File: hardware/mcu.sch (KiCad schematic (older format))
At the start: 27 parts

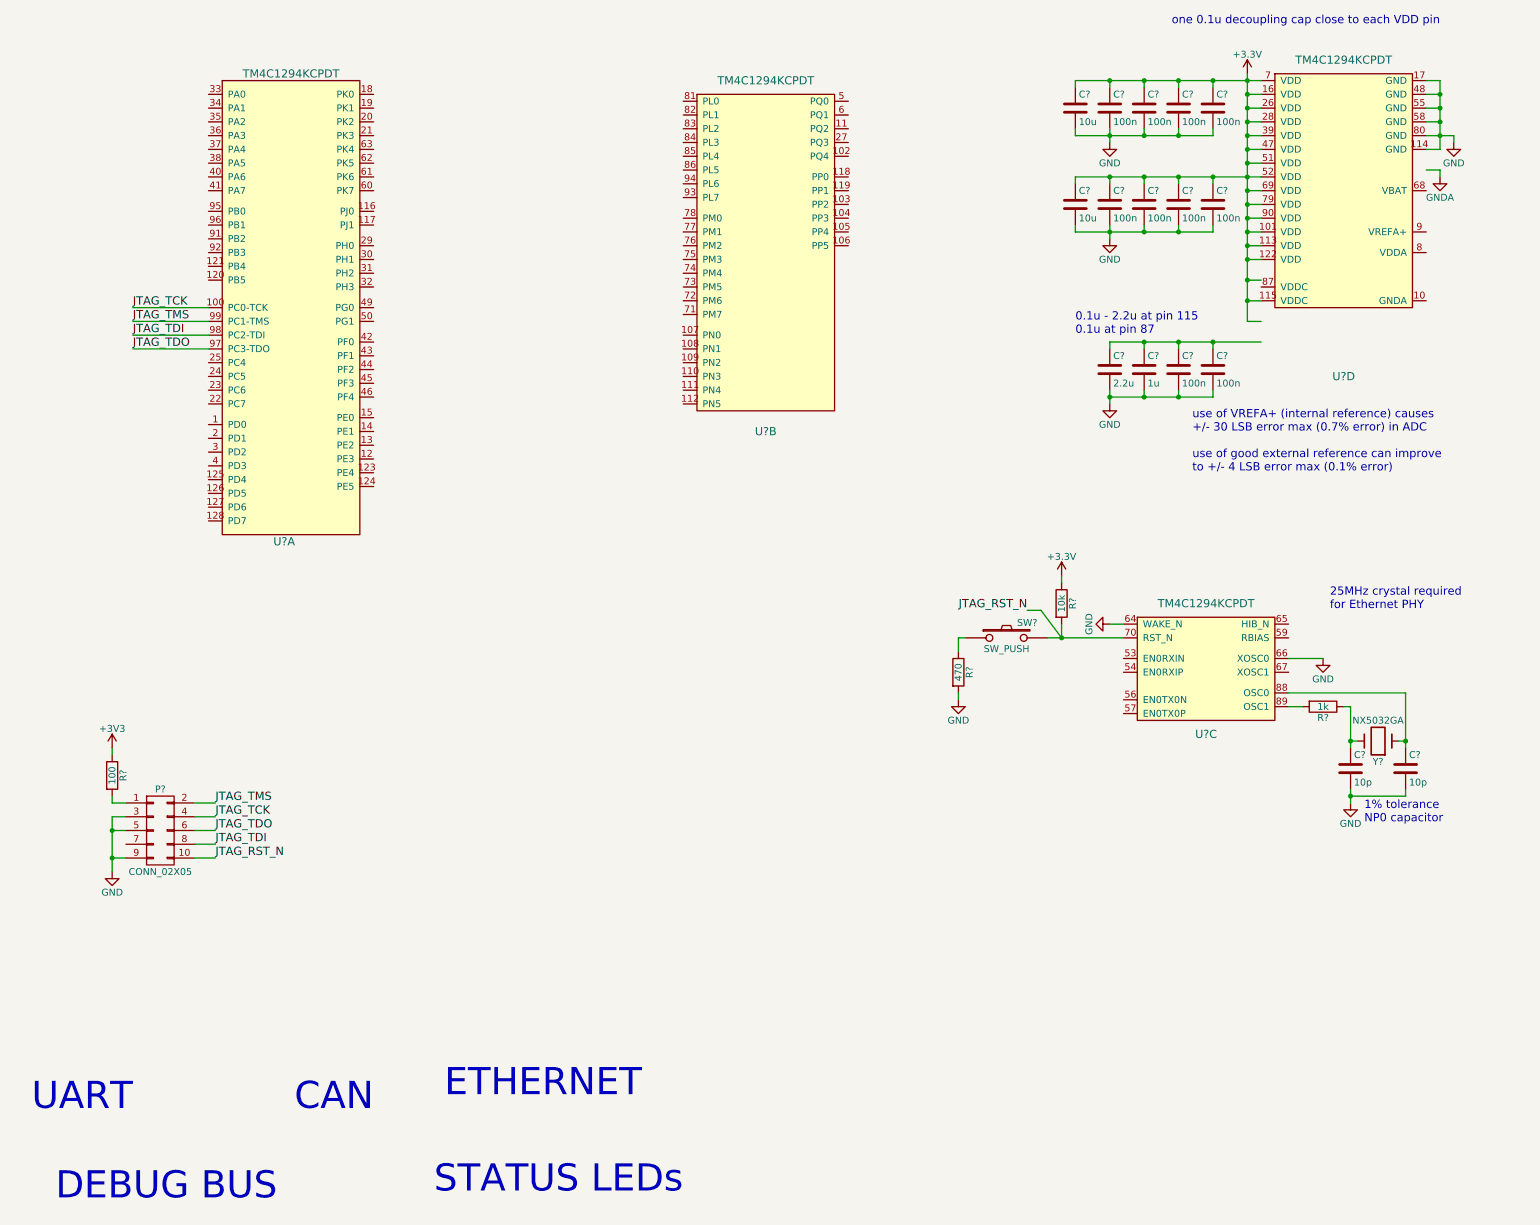
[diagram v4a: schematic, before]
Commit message: ERC cleanup, begin pcbnew population
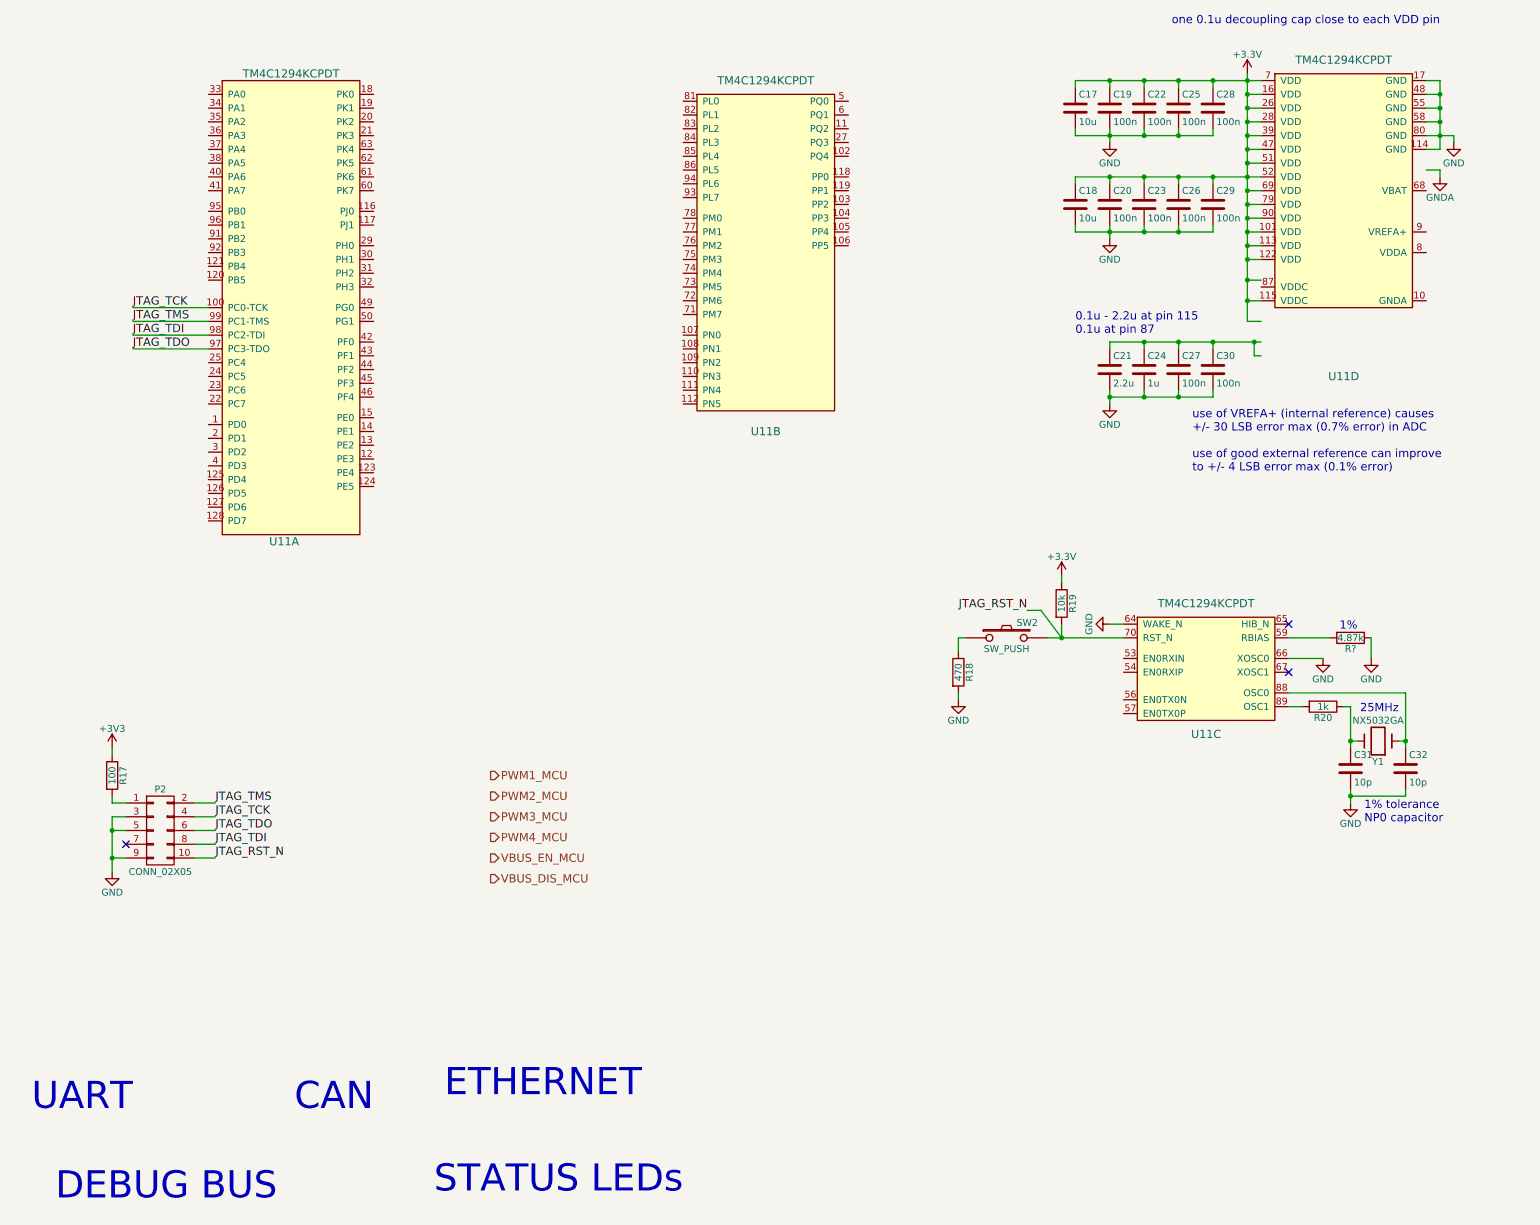
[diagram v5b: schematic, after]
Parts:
- added R?: 4.87k, symbol R
- C17, C18, C19, C20, C21, C22, C23, C24, C25, C26, C27, C28, C29, C30, C31, C32: renamed from C?; footprint (none) -> Capacitors_SMD:C_0603
- R17, R18, R19, R20: renamed from R?; footprint (none) -> Resistors_SMD:R_0603
- U11: renamed from U?; footprint (none) -> Housings_QFP:TQFP-128_14x14mm_Pitch0.4mm
- gave numbers to parts that had none: 3
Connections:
- net labels added: PWM1_MCU, PWM2_MCU, PWM3_MCU, PWM4_MCU, VBUS_DIS_MCU, VBUS_EN_MCU
- wire segments 147 -> 100
- no-connect marks 0 -> 3
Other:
- note added: "1%"
- note added: "25MHz"
- note removed: "25MHz crystal required\nfor Ethernet PHY"

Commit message: hw: minor tweaks
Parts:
- R16: renamed from R?; footprint (none) -> Resistors_SMD:R_0603
- Y1: footprint (none) -> 2kwMotorController:NX5032GA-CRYSTAL
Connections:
- net labels added: FAULT_1, FAULT_2, FAULT_3, PWM2, PWM3, PWM4, PWM5, PWM6, PWM7, QEI_IDX, QEI_PHA, QEI_PHB
- wire segments 100 -> 112
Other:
- note added: "PWM MAPPING MUST BE DESIGNED\nFOR ALL 3 DRIVE MODES W / DEAD-BAND"
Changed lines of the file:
@@
 F 0 "Y1" H 10350 6000 50  0000 C CNN
 F 1 "NX5032GA" H 10350 5700 50  0000 C CNN
-F 2 "" H 10350 5850 50  0001 C CNN
+F 2 "2kwMotorController:NX5032GA-CRYSTAL" H 10350 5850 50  0001 C CNN
 F 3 "" H 10350 5850 50  0000 C CNN
 	1    10350 5850
@@
 NoConn ~ 9700 5350
 $Comp
-L R R?
+L R R16
 U 1 1 59ABFFC0
 P 10150 5100
-F 0 "R?" V 10230 5100 50  0000 C CNN
+F 0 "R16" V 10230 5100 50  0000 C CNN
 F 1 "4.87k" V 10150 5100 50  0000 C CNN
-F 2 "" V 10080 5100 50  0000 C CNN
+F 2 "Resistors_SMD:R_0603" V 10080 5100 50  0001 C CNN
 F 3 "" H 10150 5100 50  0000 C CNN
 	1    10150 5100
@@
 $EndComp
 $Comp
-L GND #PWR?
+L GND #PWR058
 U 1 1 59AC0041
 P 10300 5250
-F 0 "#PWR?" H 10300 5000 50  0001 C CNN
+F 0 "#PWR058" H 10300 5000 50  0001 C CNN
 F 1 "GND" H 10300 5100 50  0000 C CNN
 F 2 "" H 10300 5250 50  0000 C CNN
@@
 Text Notes 10200 5050 2    60   ~ 0
 1%
+Wire Wire Line
+	3050 1750 3200 1750
+Text Label 3200 1750 0    60   ~ 0
+FAULT_1
+Wire Wire Line
+	3050 1850 3200 1850
+Text Label 3200 1850 0    60   ~ 0
+FAULT_2
+Wire Wire Line
+	5300 1200 5150 1200
+Text Label 5150 1200 2    60   ~ 0
+FAULT_3
+Wire Wire Line
+	3050 3150 3200 3150
+Text Label 3200 3150 0    60   ~ 0
+PWM2
+Wire Wire Line
+	3050 3250 3200 3250
+Text Label 3200 3250 0    60   ~ 0
+PWM3
+Wire Wire Line
+	3050 2700 3200 2700
+Text Label 3200 2700 0    60   ~ 0
+PWM4
+Wire Wire Line
+	3050 2800 3200 2800
+Text Label 3200 2800 0    60   ~ 0
+PWM5
+Wire Wire Line
+	3050 1550 3200 1550
+Wire Wire Line
+	3050 1650 3200 1650
+Text Label 3200 1550 0    60   ~ 0
+PWM6
+Text Label 3200 1650 0    60   ~ 0
+PWM7
+Text Notes 5200 2800 2    79   ~ 16
+PWM MAPPING MUST BE DESIGNED\nFOR ALL 3 DRIVE MODES W / DEAD-BAND
+Wire Wire Line
+	5300 1500 5150 1500
+Wire Wire Line
+	5300 1300 5150 1300
+Wire Wire Line
+	5150 1400 5300 1400
+Text Label 5150 1300 2    60   ~ 0
+QEI_PHA
+Text Label 5150 1400 2    60   ~ 0
+QEI_PHB
+Text Label 5150 1500 2    60   ~ 0
+QEI_IDX
 $EndSCHEMATC

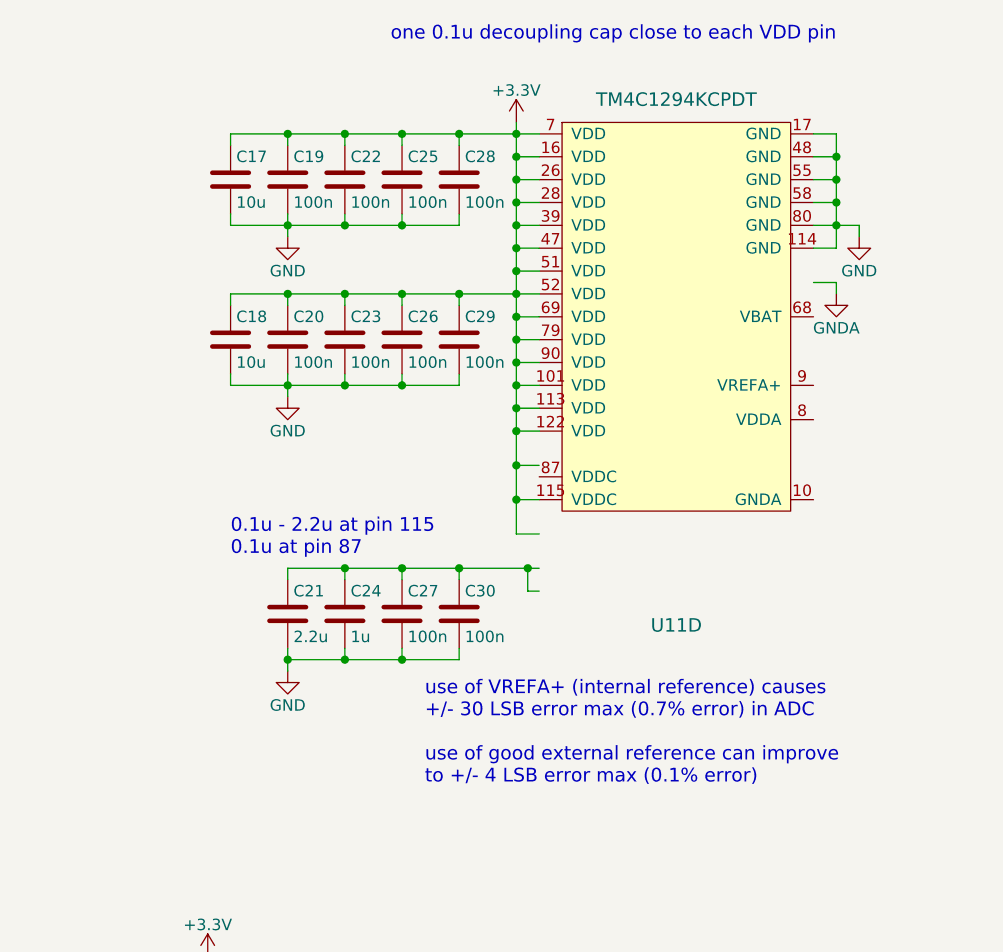
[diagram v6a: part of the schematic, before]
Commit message: Improved current sensor and simplified power supplies
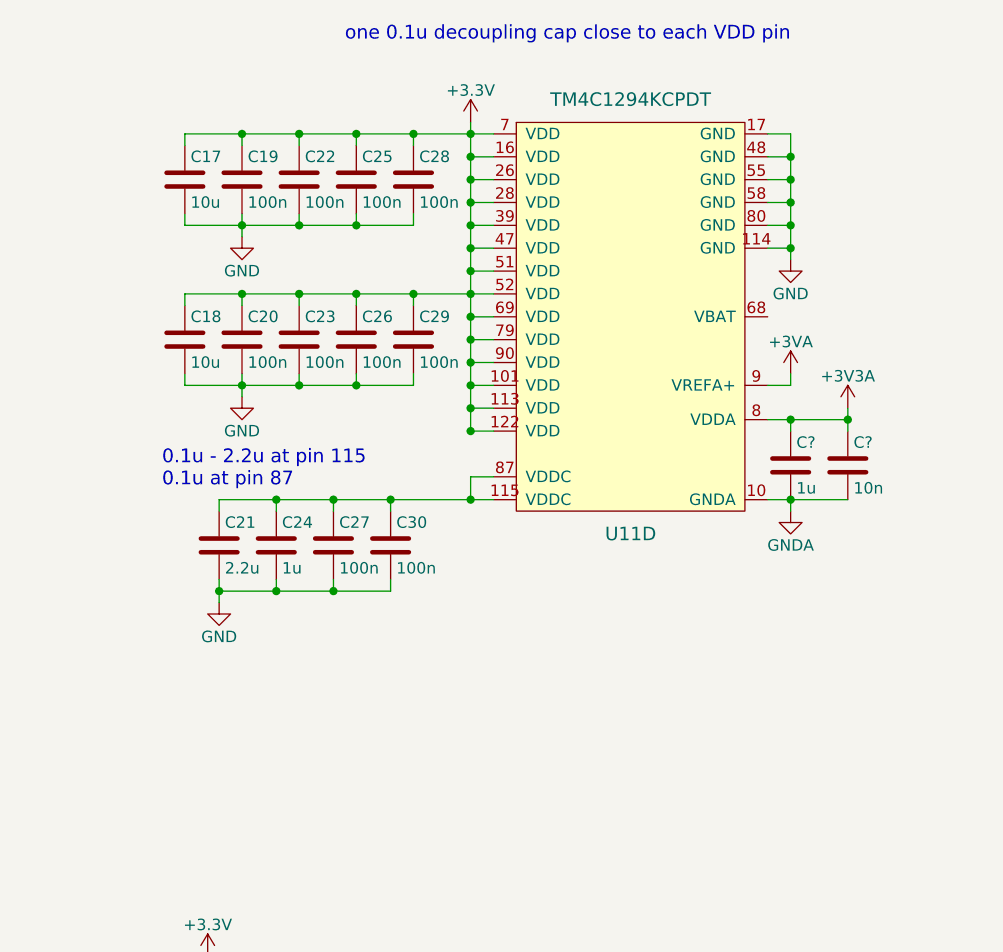
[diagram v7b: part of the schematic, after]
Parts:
- added C?: 10n, symbol C
- added C?: 1u, symbol C
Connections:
- net labels added: +3V3A, +3VA
- wire segments 112 -> 113
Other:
- note removed: "use of VREFA+ (internal reference) causes\n+/- 30 LSB error max (0.7% error) in ADC\n\nuse of good external reference can improve\nto +/- 4 LSB error max (0.1% error)"
- moved on the sheet: C17, C18, C19, C20, C21, C22, C23, C24, C25, C26, C27, C28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
